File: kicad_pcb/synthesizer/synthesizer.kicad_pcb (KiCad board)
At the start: 2 copper layers, 69.9 x 64.5 mm, 44 parts, among them J1 SCL_GND_SCA, J2 Fuente5V, J3 Fuente5V, J4 Fuente12V, J5 CONSMA006.062-G, Q1 BCW31_

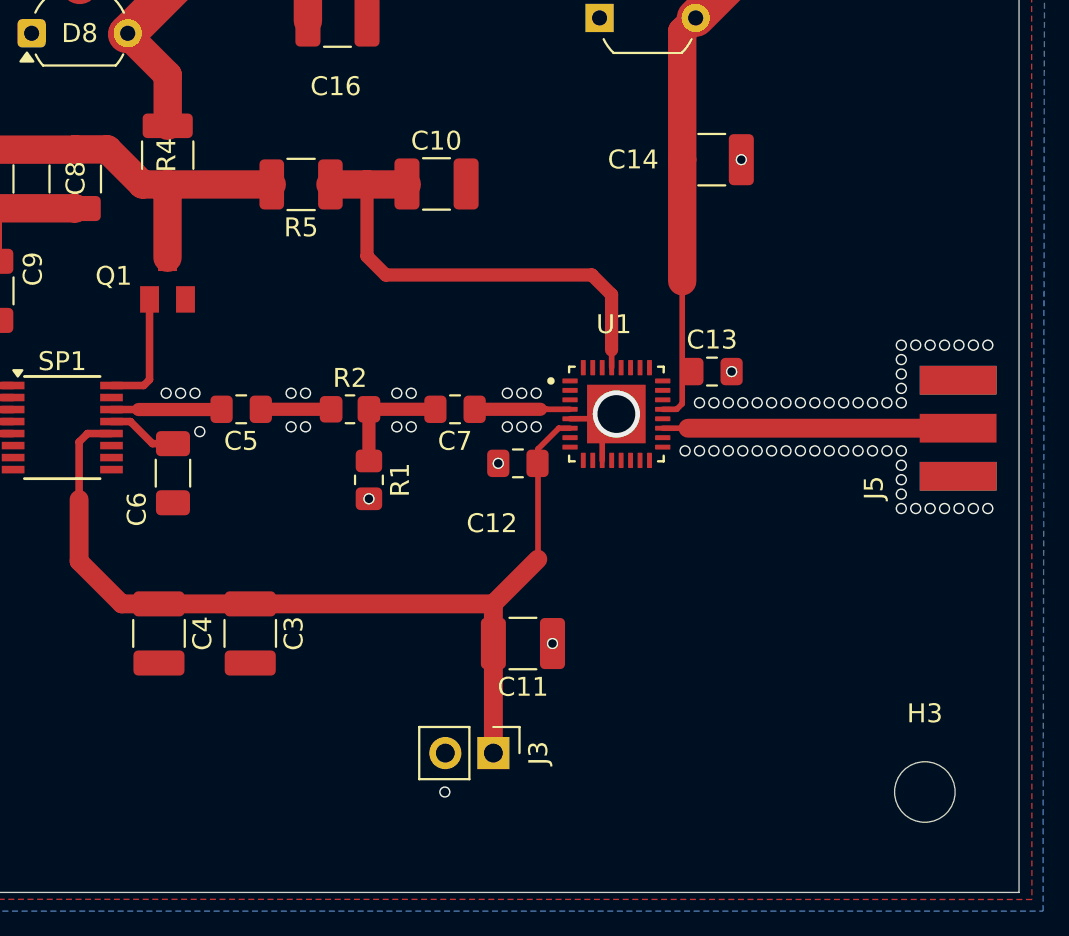
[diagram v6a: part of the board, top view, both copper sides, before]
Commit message: Cambio de huella R4
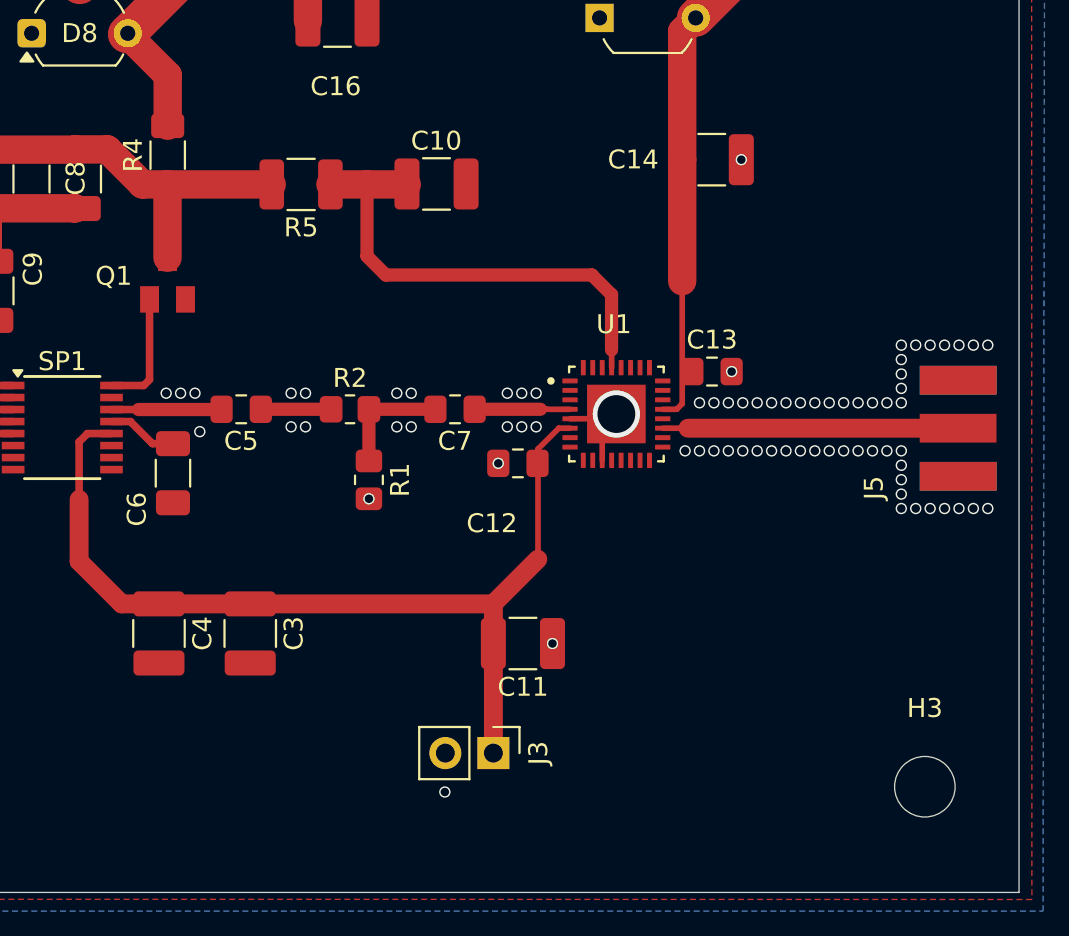
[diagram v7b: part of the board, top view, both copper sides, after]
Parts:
- R4: footprint Resistor_SMD:R_1210_3225Metric_Pad1.30x2.65mm_HandSolder -> Resistor_SMD:R_1206_3216Metric_Pad1.30x1.75mm_HandSolder
- moved H3 0.28 mm to (210.0, 123.2)
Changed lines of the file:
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@@
 	(footprint "MountingHole:MountingHole_3.2mm_M3"
 		(layer "F.Cu")
-		(at 210.0326 123.444)
+		(at 210.0326 123.1646)
 		(descr "Mounting Hole 3.2mm, M3, no annular, generated by kicad-footprint-generator mountinghole.py")
 		(tags "mountinghole M3")
@@
 		)
 		(property "Value" "MountingHole"
-			(at 0 4.15 0)
+			(at -5.08 -0.4826 90)
 			(layer "F.Fab")
 			(effects
@@
 		)
 		(property "Value" "12V"
-			(at -1.8542 -4.5212 0)
+			(at -2.667 -2.972549 0)
 			(layer "F.Fab")
 			(effects
@@
 		)
 	)
-	(footprint "Resistor_SMD:R_1210_3225Metric_Pad1.30x2.65mm_HandSolder"
+	(footprint "Resistor_SMD:R_1206_3216Metric_Pad1.30x1.75mm_HandSolder"
 		(layer "F.Cu")
 		(at 170.0067 89.7763 90)
-		(descr "Resistor SMD 1210 (3225 Metric), square (rectangular) end terminal, IPC-7351 nominal with elongated pad for handsoldering. (Body size source: IPC-SM-782 page 72, https://www.pcb-3d.com/wordpress/wp-content/uploads/ipc-sm-782a_amendment_1_and_2.pdf), generated with kicad-footprint-generator")
+		(descr "Resistor SMD 1206 (3216 Metric), square (rectangular) end terminal, IPC-7351 nominal with elongated pad for handsoldering. (Body size source: IPC-SM-782 page 72, https://www.pcb-3d.com/wordpress/wp-content/uploads/ipc-sm-782a_amendment_1_and_2.pdf), generated with kicad-footprint-generator")
 		(tags "resistor handsolder")
 		(property "Reference" "R4"
-			(at -0.0006 -0.0606 90)
+			(at 0 -1.83 90)
 			(layer "F.SilkS")
 			(effects
@@
 		)
 		(property "Value" "22k"
-			(at 0 2.28 90)
+			(at 0 1.83 90)
 			(layer "F.Fab")
 			(effects
@@
 		(attr smd)
 		(fp_line
-			(start -0.723737 -1.355)
-			(end 0.723737 -1.355)
+			(start -0.727064 -0.91)
+			(end 0.727064 -0.91)
 			(stroke
 				(width 0.12)
@@
 		)
 		(fp_line
-			(start -0.723737 1.355)
-			(end 0.723737 1.355)
+			(start -0.727064 0.91)
+			(end 0.727064 0.91)
 			(stroke
 				(width 0.12)
@@
 		)
 		(fp_line
-			(start 2.45 -1.58)
-			(end 2.45 1.58)
+			(start 2.45 -1.13)
+			(end 2.45 1.13)
 			(stroke
 				(width 0.05)
@@
 		)
 		(fp_line
-			(start -2.45 -1.58)
-			(end 2.45 -1.58)
+			(start -2.45 -1.13)
+			(end 2.45 -1.13)
 			(stroke
 				(width 0.05)
@@
 		)
 		(fp_line
-			(start 2.45 1.58)
-			(end -2.45 1.58)
+			(start 2.45 1.13)
+			(end -2.45 1.13)
 			(stroke
 				(width 0.05)
@@
 		)
 		(fp_line
-			(start -2.45 1.58)
-			(end -2.45 -1.58)
+			(start -2.45 1.13)
+			(end -2.45 -1.13)
 			(stroke
 				(width 0.05)
@@
 		)
 		(fp_line
-			(start 1.6 -1.245)
-			(end 1.6 1.245)
+			(start 1.6 -0.8)
+			(end 1.6 0.8)
 			(stroke
 				(width 0.1)
@@
 		)
 		(fp_line
-			(start -1.6 -1.245)
-			(end 1.6 -1.245)
+			(start -1.6 -0.8)
+			(end 1.6 -0.8)
 			(stroke
 				(width 0.1)
@@
 		)
 		(fp_line
-			(start 1.6 1.245)
-			(end -1.6 1.245)
+			(start 1.6 0.8)
+			(end -1.6 0.8)
 			(stroke
 				(width 0.1)
@@
 		)
 		(fp_line
-			(start -1.6 1.245)
-			(end -1.6 -1.245)
+			(start -1.6 0.8)
+			(end -1.6 -0.8)
 			(stroke
 				(width 0.1)
@@
 		)
 		(pad "1" smd roundrect
-			(at -1.55 -0.0098 90)
-			(size 1.3 2.65)
+			(at -1.55 0 90)
+			(size 1.3 1.75)
 			(layers "F.Cu" "F.Mask" "F.Paste")
 			(roundrect_rratio 0.192308)
@@
 		(pad "2" smd roundrect
 			(at 1.55 0 90)
-			(size 1.3 2.65)
+			(size 1.3 1.75)
 			(layers "F.Cu" "F.Mask" "F.Paste")
 			(roundrect_rratio 0.192308)
@@
 		)
 		(embedded_fonts no)
-		(model "${KICAD9_3DMODEL_DIR}/Resistor_SMD.3dshapes/R_1210_3225Metric.step"
+		(model "${KICAD9_3DMODEL_DIR}/Resistor_SMD.3dshapes/R_1206_3216Metric.step"
 			(offset
 				(xyz 0 0 0)
@@
 		)
 		(property "Value" "4.7V"
-			(at -4.953 -0.381 0)
+			(at -3.429 0.0762 0)
 			(layer "F.Fab")
 			(effects
@@
 		)
 		(property "Value" "MountingHole"
-			(at 0 4.15 0)
+			(at -0.5588 4.191 0)
 			(layer "F.Fab")
 			(effects

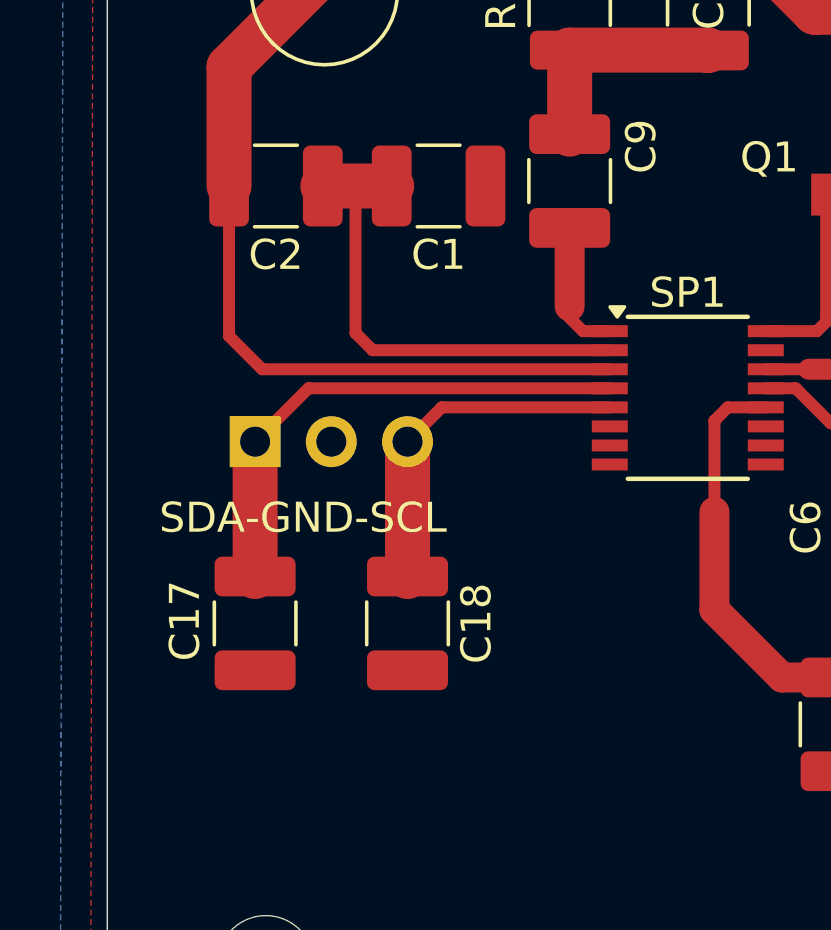
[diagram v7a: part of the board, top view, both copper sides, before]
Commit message: Lineas SDA/SCL
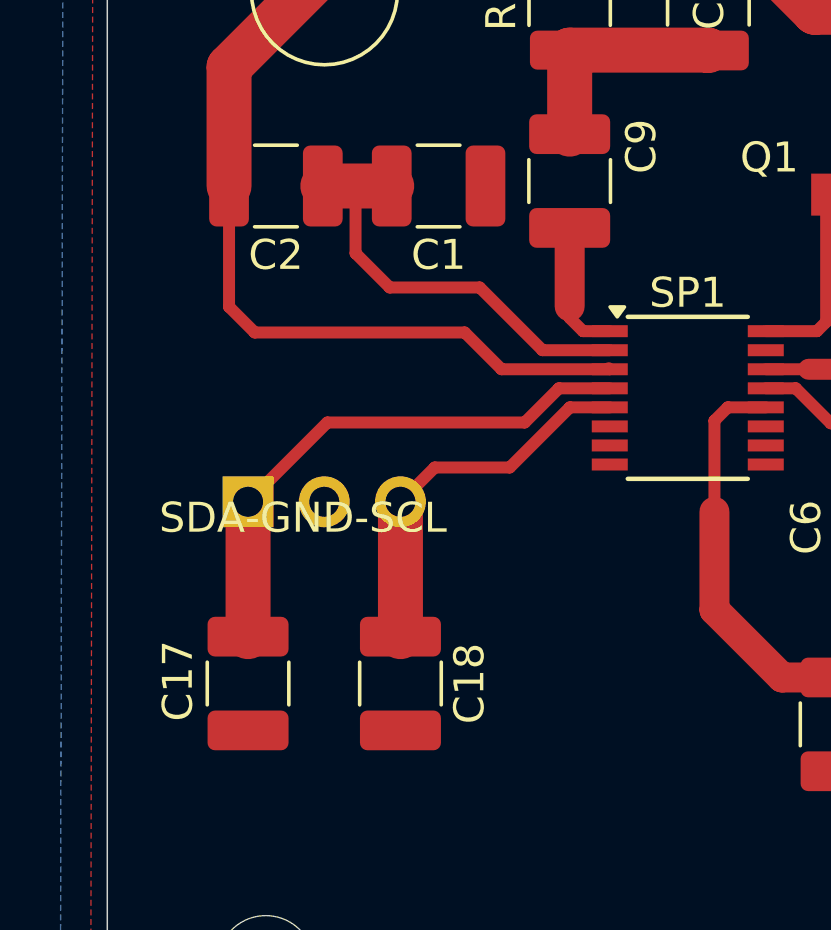
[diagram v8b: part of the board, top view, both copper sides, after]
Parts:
- moved C17 2.02 mm to (149.8, 113.7)
- moved J1 2.02 mm to (149.8, 107.6)
- moved C18 2.02 mm to (154.9, 113.7)
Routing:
- net Net-(SP1-Crystal_Cap): track 15.9 -> 14.4 mm
- net Net-(J1-Pin_1): track 17.1 -> 18.1 mm
- net Net-(J1-Pin_3): track 11.7 -> 12.8 mm
- net Net-(SP1-Crystal): track 26.6 -> 26.1 mm
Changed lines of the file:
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@@
 	(footprint "Capacitor_SMD:C_1210_3225Metric_Pad1.33x2.70mm_HandSolder"
 		(layer "F.Cu")
-		(at 150.0124 111.6969 -90)
+		(at 149.777 113.7013 -90)
 		(descr "Capacitor SMD 1210 (3225 Metric), square (rectangular) end terminal, IPC-7351 nominal with elongated pad for handsoldering. (Body size source: IPC-SM-782 page 76, https://www.pcb-3d.com/wordpress/wp-content/uploads/ipc-sm-782a_amendment_1_and_2.pdf), generated with kicad-footprint-generator")
 		(tags "capacitor handsolder")
@@
 	(footprint "Capacitor_SMD:C_1210_3225Metric_Pad1.33x2.70mm_HandSolder"
 		(layer "F.Cu")
-		(at 155.0924 111.6969 -90)
+		(at 154.857 113.7013 -90)
 		(descr "Capacitor SMD 1210 (3225 Metric), square (rectangular) end terminal, IPC-7351 nominal with elongated pad for handsoldering. (Body size source: IPC-SM-782 page 76, https://www.pcb-3d.com/wordpress/wp-content/uploads/ipc-sm-782a_amendment_1_and_2.pdf), generated with kicad-footprint-generator")
 		(tags "capacitor handsolder")
@@
 	(footprint "Connector_PinHeader_2.54mm:PinHeader_1x03_P2.54mm_Vertical"
 		(layer "B.Cu")
-		(at 150.0124 105.6386 -90)
+		(at 149.777 107.643 -90)
 		(descr "Through hole straight pin header, 1x03, 2.54mm pitch, single row")
 		(tags "Through hole pin header THT 1x03 2.54mm single row")
@@
 	)
 	(segment
+		(start 161.8343 103.2256)
+		(end 158.2256 103.2256)
+		(width 0.399999)
+		(layer "F.Cu")
+		(net 8)
+	)
+	(segment
 		(start 149.1435 97.1169)
 		(end 149.1435 93.1471)
@@
 	)
 	(segment
-		(start 161.8343 103.2256)
-		(end 150.2484 103.2256)
+		(start 149.1435 101.1435)
+		(end 149.1435 97.1169)
 		(width 0.399999)
 		(layer "F.Cu")
@@
 	)
 	(segment
-		(start 150.2484 103.2256)
-		(end 149.1435 102.1207)
+		(start 158.2256 103.2256)
+		(end 157 102)
 		(width 0.399999)
 		(layer "F.Cu")
@@
 	)
 	(segment
-		(start 149.1435 102.1207)
-		(end 149.1435 97.1169)
+		(start 157 102)
+		(end 150 102)
+		(width 0.399999)
+		(layer "F.Cu")
+		(net 8)
+	)
+	(segment
+		(start 150 102)
+		(end 149.1435 101.1435)
+		(width 0.399999)
+		(layer "F.Cu")
+		(net 8)
+	)
+	(segment
+		(start 161.8343 103.2256)
+		(end 161.8003 103.1916)
 		(width 0.399999)
 		(layer "F.Cu")
@@
 	)
 	(segment
-		(start 153.3599 102.0191)
-		(end 153.3599 97.1169)
+		(start 154.5 100.5)
+		(end 153.3599 99.3599)
 		(width 0.399999)
 		(layer "F.Cu")
@@
 	)
 	(segment
-		(start 153.9314 102.5906)
-		(end 153.3599 102.0191)
+		(start 152.2685 97.1169)
+		(end 154.566 97.1169)
+		(width 1.5)
+		(layer "F.Cu")
+		(net 14)
+	)
+	(segment
+		(start 161.8343 102.5906)
+		(end 159.5906 102.5906)
 		(width 0.399999)
 		(layer "F.Cu")
@@
 	)
 	(segment
-		(start 152.2685 97.1169)
-		(end 154.566 97.1169)
-		(width 1.5)
+		(start 159.5906 102.5906)
+		(end 157.5 100.5)
+		(width 0.399999)
 		(layer "F.Cu")
 		(net 14)
 	)
 	(segment
-		(start 161.8343 102.5906)
-		(end 153.9314 102.5906)
+		(start 157.5 100.5)
+		(end 154.5 100.5)
+		(width 0.399999)
+		(layer "F.Cu")
+		(net 14)
+	)
+	(segment
+		(start 153.3599 99.3599)
+		(end 153.3599 97.1169)
 		(width 0.399999)
 		(layer "F.Cu")
@@
 	)
 	(segment
-		(start 161.8343 104.4956)
-		(end 156.2354 104.4956)
+		(start 158.5 106.5)
+		(end 160.5044 104.4956)
 		(width 0.399999)
 		(layer "F.Cu")
@@
 	)
 	(segment
-		(start 155.0924 105.6386)
-		(end 155.0924 110.1344)
+		(start 154.857 107.643)
+		(end 154.857 112.1388)
 		(width 1.5)
 		(layer "F.Cu")
@@
 	)
 	(segment
-		(start 156.2354 104.4956)
-		(end 155.0924 105.6386)
+		(start 154.857 107.643)
+		(end 156 106.5)
+		(width 0.399999)
+		(layer "F.Cu")
+		(net 50)
+	)
+	(segment
+		(start 160.5044 104.4956)
+		(end 161.8343 104.4956)
 		(width 0.399999)
 		(layer "F.Cu")
@@
 	)
 	(segment
-		(start 161.8343 103.8606)
-		(end 151.7904 103.8606)
+		(start 156 106.5)
+		(end 158.5 106.5)
+		(width 0.399999)
+		(layer "F.Cu")
+		(net 50)
+	)
+	(segment
+		(start 160.1394 103.8606)
+		(end 161.8343 103.8606)
+		(width 0.399999)
+		(layer "F.Cu")
+		(net 51)
+	)
+	(segment
+		(start 159 105)
+		(end 160.1394 103.8606)
+		(width 0.399999)
+		(layer "F.Cu")
+		(net 51)
+	)
+	(segment
+		(start 152.42 105)
+		(end 159 105)
 		(width 0.399999)
 		(layer "F.Cu")
@@
 	)
 	(segment
-		(start 151.7904 103.8606)
-		(end 150.0124 105.6386)
+		(start 149.777 107.643)
+		(end 152.42 105)
 		(width 0.399999)
 		(layer "F.Cu")
@@
 	)
 	(segment
-		(start 150.0124 105.6386)
-		(end 150.0124 110.1344)
+		(start 149.777 107.643)
+		(end 149.777 112.1388)
 		(width 1.5)
 		(layer "F.Cu")
